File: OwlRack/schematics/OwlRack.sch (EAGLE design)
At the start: 77 parts, among them IC1 THAT1646, IC2 THAT1646, IC3 LM317MABT, IC5 NE5532N, J4 NEUTRIK_NMJ6HCD2, J5 NEUTRIK_NMJ6HCD2

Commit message: changed connector and 5v reg
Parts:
- removed C18: 1u, rcl:CPOL-EUE2.5-7
- removed IC3: LM317MABT, v-reg:LM317MABT
- removed J5: NEUTRIK_NMJ6HCD2, neutrik_jacks:NEUTRIK_NMJ6HCD2
- removed LEFT, RIGHT: NCJ10FI-H, con-neutrik_ag:NCJ10FI-H
- removed R6: 1k, Rebel:R-EU_0204/7
- removed R7: 330R, Rebel:R-EU_0204/7
- added IN3: (no value), SparkFun:M02PTH
- added J1, J2, J3: NEUTRIK_NRJ6HFSTD, neutrik_jacks:NEUTRIK_NRJ6HFSTD
- added U$2: REG_S9V11F5, Rebel:REG_S9V11F5
- J4: value NEUTRIK_NMJ6HCD2 -> NEUTRIK_NRJ6HFSTD; device neutrik_jacks:NEUTRIK_NMJ6HCD2 -> neutrik_jacks:NEUTRIK_NRJ6HFSTD
- UART: device SparkFun:M03PTH -> Rebel:CON-JST-1X03PH-TH
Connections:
- removed net N$11: C18.+, IC3.ADJ, R6.2, R7.1
- new net N$6: J1.R, J2.TN
- net +12V: now also U$2.VIN; no longer IC3.IN
- net +5V: now also U$2.VOUT; no longer IC3.OUT, R7.2
- net FX_IN_L: now also J1.T; no longer J4.T, J5.TN
- net FX_IN_R: now also J2.T; no longer J5.T
- net GND: now also IN3.2, U$2.GND; no longer C18.-, J4.S, J4.TN, J5.S, R300.1, R301.1, R6.1
- net GNDA: now also IN3.1, J1.RN, J1.S, J1.SN, J1.TN, J2.RN, J2.S, J2.SN, J3.S, J4.S, R300.1, R301.1; no longer LEFT.1, LEFT.G, LEFT.S, LEFT.SS, RIGHT.1, RIGHT.G, RIGHT.S, RIGHT.SS
- net N$18: now also J3.R; no longer RIGHT.2, RIGHT.T
- net N$19: now also J3.T; no longer RIGHT.3, RIGHT.R
- net N$2: now also J4.R; no longer LEFT.2, LEFT.T
- net N$3: now also J4.T; no longer LEFT.3, LEFT.R
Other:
- note added: "Copyright 2017 Rebel Technology"
- note added: "OWL Rack Rev03"
- note removed: "Copyright 2016 Rebel Technology"
- note removed: "OWL Rack Revision 2"
- moved on the sheet: C1, C10, C11, C12, C13, C14, C15, C16, C2, C3, C300, C301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

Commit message: boards sent for production
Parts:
- added IN4, IN5: (no value), SparkFun:M02PTH
- renumbered U$2 to IC3
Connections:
- net GND: now also IN4.2, IN5.2
- net GNDA: now also IN4.1, IN5.1
- net N$18: now also J4.R; no longer J3.R
- net N$19: now also J4.T; no longer J3.T
- net N$2: now also J3.R; no longer J4.R
- net N$3: now also J3.T; no longer J4.T
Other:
- moved on the sheet: J3, J4
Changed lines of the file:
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@@
 <part name="J1" library="neutrik_jacks" deviceset="NEUTRIK_NRJ6HF" device="STD"/>
 <part name="J2" library="neutrik_jacks" deviceset="NEUTRIK_NRJ6HF" device="STD"/>
+<part name="J4" library="neutrik_jacks" deviceset="NEUTRIK_NRJ6HF" device="STD"/>
 <part name="J3" library="neutrik_jacks" deviceset="NEUTRIK_NRJ6HF" device="STD"/>
-<part name="J4" library="neutrik_jacks" deviceset="NEUTRIK_NRJ6HF" device="STD"/>
 <part name="UART" library="Rebel" deviceset="CON-JST-1X03" device="PH-TH"/>
-<part name="U$2" library="Rebel" deviceset="REG_S9V11F5" device=""/>
+<part name="IC3" library="Rebel" deviceset="REG_S9V11F5" device=""/>
 <part name="GND5" library="supply1" deviceset="GNDA" device=""/>
 <part name="GND17" library="supply1" deviceset="GNDA" device=""/>
@@
 <part name="GND22" library="supply1" deviceset="GND" device=""/>
 <part name="GND35" library="supply1" deviceset="GNDA" device=""/>
+<part name="IN4" library="SparkFun" deviceset="M02" device="PTH"/>
+<part name="IN5" library="SparkFun" deviceset="M02" device="PTH"/>
 </parts>
 <sheets>
@@
 <instance part="J1" gate="J" x="-45.72" y="101.6"/>
 <instance part="J2" gate="J" x="-45.72" y="55.88"/>
-<instance part="J3" gate="J" x="360.68" y="162.56" rot="R180"/>
-<instance part="J4" gate="J" x="360.68" y="83.82" rot="R180"/>
+<instance part="J4" gate="J" x="360.68" y="162.56" rot="R180"/>
+<instance part="J3" gate="J" x="360.68" y="83.82" rot="R180"/>
 <instance part="UART" gate="G$1" x="195.58" y="81.28"/>
-<instance part="U$2" gate="G$1" x="71.12" y="177.8"/>
+<instance part="IC3" gate="G$1" x="71.12" y="177.8"/>
 <instance part="GND5" gate="1" x="-10.16" y="81.28"/>
 <instance part="GND17" gate="1" x="-33.02" y="35.56"/>
@@
 <instance part="GND22" gate="1" x="-7.62" y="-12.7" rot="MR0"/>
 <instance part="GND35" gate="1" x="-12.7" y="-12.7"/>
+<instance part="IN4" gate="G$1" x="5.08" y="-5.08" rot="R180"/>
+<instance part="IN5" gate="G$1" x="5.08" y="-22.86" rot="R180"/>
 </instances>
 <busses>
@@
 <pinref part="IN2" gate="G$1" pin="2"/>
 <pinref part="GND23" gate="1" pin="GND"/>
-<wire x1="-5.08" y1="-25.4" x2="-7.62" y2="-25.4" width="0.1524" layer="91"/>
+<wire x1="-2.54" y1="-25.4" x2="-7.62" y2="-25.4" width="0.1524" layer="91"/>
 <wire x1="-7.62" y1="-25.4" x2="-7.62" y2="-27.94" width="0.1524" layer="91"/>
+<pinref part="IN5" gate="G$1" pin="2"/>
+<junction x="-2.54" y="-25.4"/>
+<wire x1="-2.54" y1="-25.4" x2="-5.08" y2="-25.4" width="0.1524" layer="91"/>
 </segment>
 <segment>
@@
 </segment>
 <segment>
-<pinref part="U$2" gate="G$1" pin="GND"/>
+<pinref part="IC3" gate="G$1" pin="GND"/>
 <pinref part="GND25" gate="1" pin="GND"/>
 <wire x1="81.28" y1="147.32" x2="81.28" y2="165.1" width="0.1524" layer="91"/>
@@
 <pinref part="IN3" gate="G$1" pin="2"/>
 <pinref part="GND22" gate="1" pin="GND"/>
-<wire x1="-5.08" y1="-7.62" x2="-7.62" y2="-7.62" width="0.1524" layer="91"/>
+<wire x1="-2.54" y1="-7.62" x2="-7.62" y2="-7.62" width="0.1524" layer="91"/>
 <wire x1="-7.62" y1="-7.62" x2="-7.62" y2="-10.16" width="0.1524" layer="91"/>
+<pinref part="IN4" gate="G$1" pin="2"/>
+<junction x="-2.54" y="-7.62"/>
+<wire x1="-2.54" y1="-7.62" x2="-5.08" y2="-7.62" width="0.1524" layer="91"/>
 </segment>
 </net>
@@
 <junction x="96.52" y="177.8"/>
 <pinref part="C17" gate="G$1" pin="+"/>
-<pinref part="U$2" gate="G$1" pin="VOUT"/>
+<pinref part="IC3" gate="G$1" pin="VOUT"/>
 </segment>
 </net>
@@
 <pinref part="P+9" gate="1" pin="+12V"/>
 <pinref part="C19" gate="G$1" pin="1"/>
-<pinref part="U$2" gate="G$1" pin="VIN"/>
+<pinref part="IC3" gate="G$1" pin="VIN"/>
 </segment>
 <segment>
@@
 <wire x1="353.06" y1="154.94" x2="347.98" y2="154.94" width="0.1524" layer="91"/>
 <pinref part="GND11" gate="1" pin="GNDA"/>
-<pinref part="J3" gate="J" pin="S"/>
+<pinref part="J4" gate="J" pin="S"/>
 </segment>
 <segment>
@@
 <wire x1="353.06" y1="76.2" x2="347.98" y2="76.2" width="0.1524" layer="91"/>
 <wire x1="347.98" y1="76.2" x2="347.98" y2="71.12" width="0.1524" layer="91"/>
-<pinref part="J4" gate="J" pin="S"/>
+<pinref part="J3" gate="J" pin="S"/>
 </segment>
 <segment>
 <pinref part="IN2" gate="G$1" pin="1"/>
 <pinref part="GND24" gate="1" pin="GNDA"/>
-<wire x1="-5.08" y1="-22.86" x2="-12.7" y2="-22.86" width="0.1524" layer="91"/>
+<wire x1="-2.54" y1="-22.86" x2="-12.7" y2="-22.86" width="0.1524" layer="91"/>
 <wire x1="-12.7" y1="-22.86" x2="-12.7" y2="-27.94" width="0.1524" layer="91"/>
+<pinref part="IN5" gate="G$1" pin="1"/>
+<junction x="-2.54" y="-22.86"/>
+<wire x1="-2.54" y1="-22.86" x2="-5.08" y2="-22.86" width="0.1524" layer="91"/>
 </segment>
 <segment>
@@
 <pinref part="IN3" gate="G$1" pin="1"/>
 <pinref part="GND35" gate="1" pin="GNDA"/>
-<wire x1="-5.08" y1="-5.08" x2="-12.7" y2="-5.08" width="0.1524" layer="91"/>
+<wire x1="-2.54" y1="-5.08" x2="-12.7" y2="-5.08" width="0.1524" layer="91"/>
 <wire x1="-12.7" y1="-5.08" x2="-12.7" y2="-10.16" width="0.1524" layer="91"/>
+<pinref part="IN4" gate="G$1" pin="1"/>
+<junction x="-2.54" y="-5.08"/>
+<wire x1="-2.54" y1="-5.08" x2="-5.08" y2="-5.08" width="0.1524" layer="91"/>
 </segment>
 </net>
@@
 <wire x1="317.5" y1="167.64" x2="317.5" y2="160.02" width="0.1524" layer="91"/>
 <junction x="317.5" y="160.02"/>
-<pinref part="J3" gate="J" pin="R"/>
+<pinref part="J4" gate="J" pin="R"/>
 </segment>
 </net>
@@
 <wire x1="266.7" y1="167.64" x2="266.7" y2="165.1" width="0.1524" layer="91"/>
 <junction x="266.7" y="165.1"/>
-<pinref part="J3" gate="J" pin="T"/>
+<pinref part="J4" gate="J" pin="T"/>
 </segment>
 </net>
@@
 <wire x1="320.04" y1="88.9" x2="320.04" y2="81.28" width="0.1524" layer="91"/>
 <junction x="320.04" y="81.28"/>
-<pinref part="J4" gate="J" pin="R"/>
+<pinref part="J3" gate="J" pin="R"/>
 </segment>
 </net>
@@
 <wire x1="269.24" y1="88.9" x2="269.24" y2="86.36" width="0.1524" layer="91"/>
 <junction x="269.24" y="86.36"/>
-<pinref part="J4" gate="J" pin="T"/>
-</segment>
-</net>
+<pinref part="J3" gate="J" pin="T"/>
+</segment>
+</net>

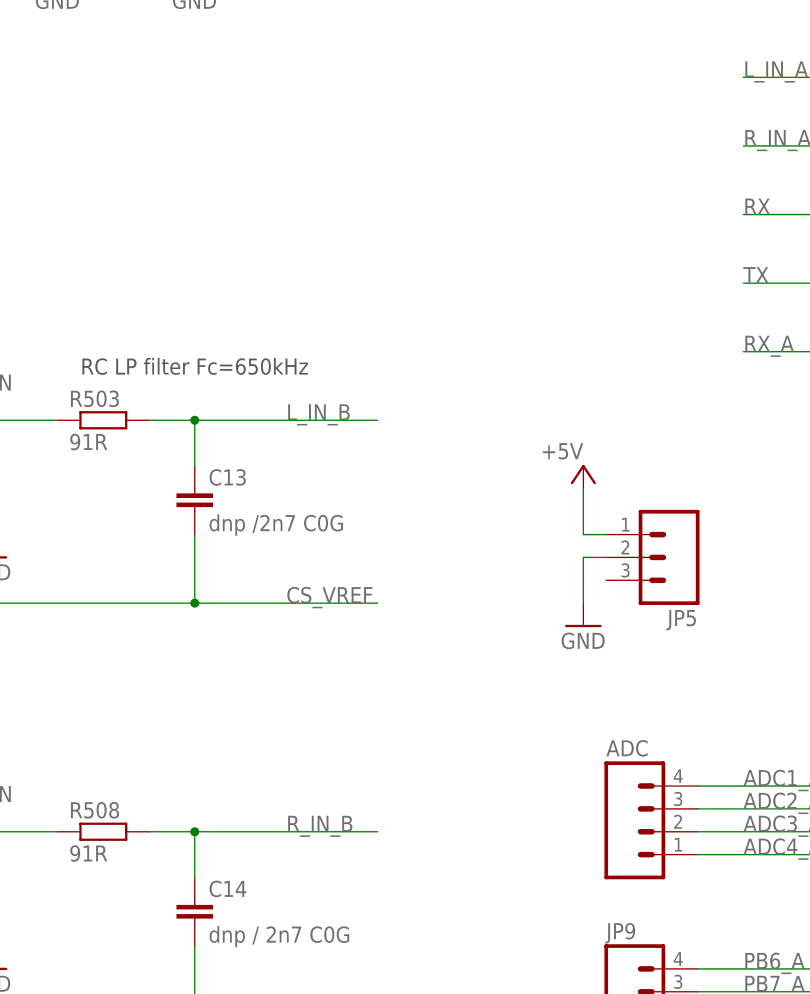
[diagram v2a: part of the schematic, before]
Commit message: Fixed mechanical OWL top board and both OWL rack boards.
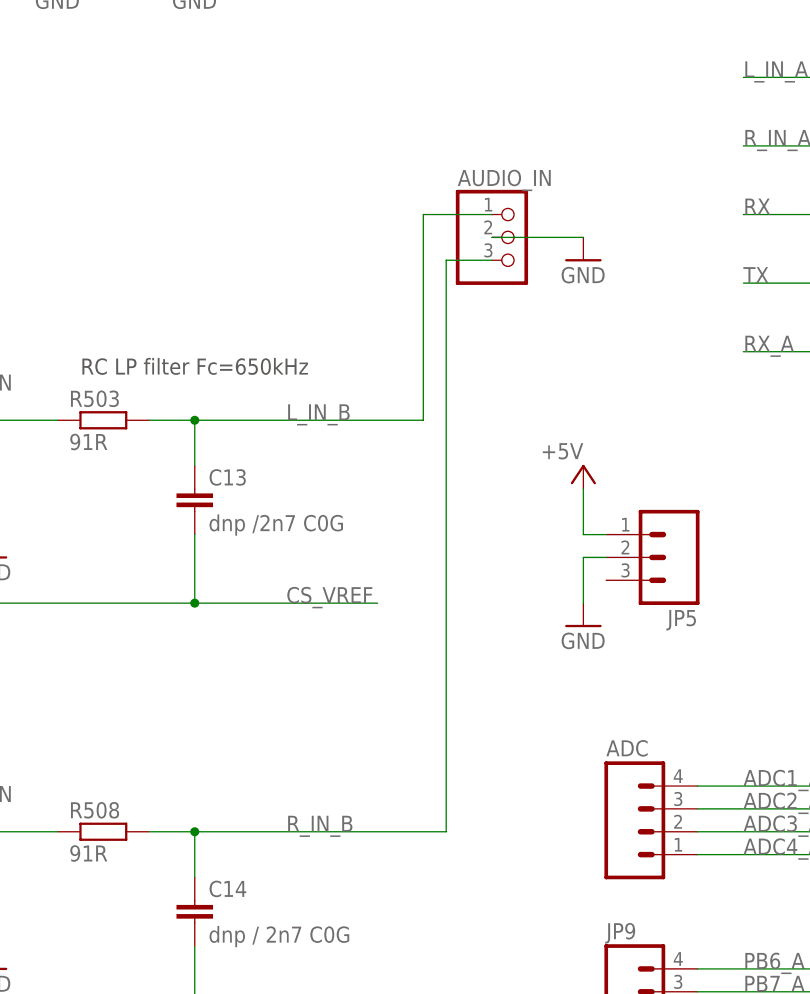
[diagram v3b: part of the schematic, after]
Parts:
- added AUDIO_IN: (no value), Rebel:CON-JST-1X03PH-TH
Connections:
- net GND: now also AUDIO_IN.2
- net L_IN_B: now also AUDIO_IN.1
- net R_IN_B: now also AUDIO_IN.3
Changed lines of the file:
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@@
 <?xml version="1.0" encoding="utf-8"?>
 <!DOCTYPE eagle SYSTEM "eagle.dtd">
-<eagle version="7.5.0">
+<eagle version="7.6.0">
 <drawing>
 <settings>
@@
 <part name="IN4" library="SparkFun" deviceset="M02" device="PTH"/>
 <part name="IN5" library="SparkFun" deviceset="M02" device="PTH"/>
+<part name="AUDIO_IN" library="Rebel" deviceset="CON-JST-1X03" device="PH-TH"/>
+<part name="GND36" library="supply1" deviceset="GND" device=""/>
 </parts>
 <sheets>
@@
 <instance part="IN4" gate="G$1" x="5.08" y="-5.08" rot="R180"/>
 <instance part="IN5" gate="G$1" x="5.08" y="-22.86" rot="R180"/>
+<instance part="AUDIO_IN" gate="G$1" x="132.08" y="116.84"/>
+<instance part="GND36" gate="1" x="139.7" y="114.3"/>
 </instances>
 <busses>
@@
 <wire x1="-2.54" y1="-7.62" x2="-5.08" y2="-7.62" width="0.1524" layer="91"/>
 </segment>
+<segment>
+<pinref part="AUDIO_IN" gate="G$1" pin="2"/>
+<pinref part="GND36" gate="1" pin="GND"/>
+<wire x1="129.54" y1="116.84" x2="139.7" y2="116.84" width="0.1524" layer="91"/>
+</segment>
 </net>
 <net name="+5V" class="0">
@@
 <wire x1="96.52" y1="45.72" x2="96.52" y2="50.8" width="0.1524" layer="91"/>
 <junction x="96.52" y="50.8"/>
-<wire x1="96.52" y1="50.8" x2="116.84" y2="50.8" width="0.1524" layer="91"/>
+<wire x1="96.52" y1="50.8" x2="124.46" y2="50.8" width="0.1524" layer="91"/>
 <pinref part="C14" gate="G$1" pin="1"/>
+<wire x1="124.46" y1="50.8" x2="124.46" y2="114.3" width="0.1524" layer="91"/>
+<pinref part="AUDIO_IN" gate="G$1" pin="3"/>
+<wire x1="124.46" y1="114.3" x2="129.54" y2="114.3" width="0.1524" layer="91"/>
 </segment>
 </net>
@@
 <junction x="96.52" y="96.52"/>
 <pinref part="R503" gate="G$1" pin="2"/>
-<wire x1="96.52" y1="96.52" x2="116.84" y2="96.52" width="0.1524" layer="91"/>
+<wire x1="96.52" y1="96.52" x2="121.92" y2="96.52" width="0.1524" layer="91"/>
 <pinref part="C13" gate="G$1" pin="1"/>
-</segment>
-</net>
+<wire x1="121.92" y1="96.52" x2="121.92" y2="119.38" width="0.1524" layer="91"/>
+<pinref part="AUDIO_IN" gate="G$1" pin="1"/>
+<wire x1="121.92" y1="119.38" x2="129.54" y2="119.38" width="0.1524" layer="91"/>
+</segment>
+</net>

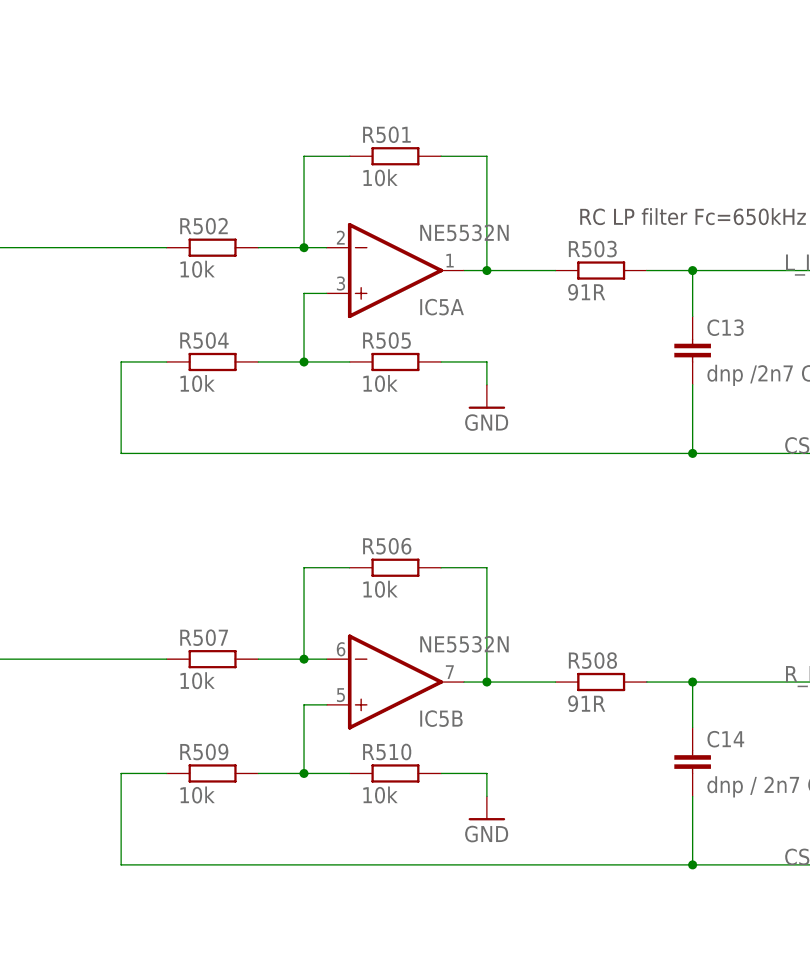
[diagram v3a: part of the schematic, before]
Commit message: changed component values
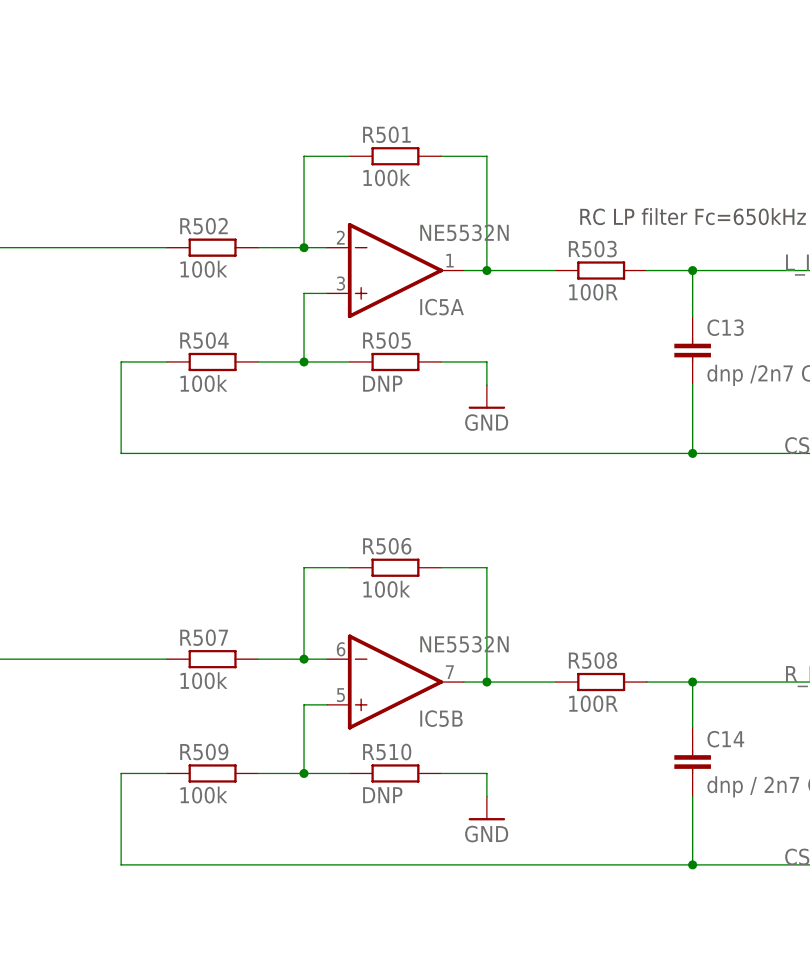
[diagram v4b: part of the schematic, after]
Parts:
- R501, R502, R504, R506, R507, R509: value 10k -> 100k
- R503, R508: value 91R -> 100R
- R505, R510: value 10k -> DNP
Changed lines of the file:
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@@
 <?xml version="1.0" encoding="utf-8"?>
 <!DOCTYPE eagle SYSTEM "eagle.dtd">
-<eagle version="7.6.0">
+<eagle version="7.5.0">
 <drawing>
 <settings>
@@
 <part name="JP11" library="SparkFun" deviceset="M02" device="PTH"/>
 <part name="JP12" library="SparkFun" deviceset="M04" device="PTH"/>
-<part name="R508" library="Rebel" deviceset="R-EU_" device="0204/7" value="91R"/>
-<part name="R503" library="Rebel" deviceset="R-EU_" device="0204/7" value="91R"/>
+<part name="R508" library="Rebel" deviceset="R-EU_" device="0204/7" value="100R"/>
+<part name="R503" library="Rebel" deviceset="R-EU_" device="0204/7" value="100R"/>
 <part name="GND26" library="supply1" deviceset="GND" device=""/>
 <part name="GND27" library="supply1" deviceset="GND" device=""/>
 <part name="P+6" library="supply1" deviceset="+12V" device=""/>
 <part name="P-1" library="supply1" deviceset="-12V" device=""/>
-<part name="R501" library="Rebel" deviceset="R-EU_" device="0204/7" value="10k"/>
-<part name="R504" library="Rebel" deviceset="R-EU_" device="0204/7" value="10k"/>
-<part name="R505" library="Rebel" deviceset="R-EU_" device="0204/7" value="10k"/>
-<part name="R502" library="Rebel" deviceset="R-EU_" device="0204/7" value="10k"/>
+<part name="R501" library="Rebel" deviceset="R-EU_" device="0204/7" value="100k"/>
+<part name="R504" library="Rebel" deviceset="R-EU_" device="0204/7" value="100k"/>
+<part name="R505" library="Rebel" deviceset="R-EU_" device="0204/7" value="DNP"/>
+<part name="R502" library="Rebel" deviceset="R-EU_" device="0204/7" value="100k"/>
 <part name="GND2" library="supply1" deviceset="GND" device=""/>
-<part name="R506" library="Rebel" deviceset="R-EU_" device="0204/7" value="10k"/>
-<part name="R509" library="Rebel" deviceset="R-EU_" device="0204/7" value="10k"/>
-<part name="R510" library="Rebel" deviceset="R-EU_" device="0204/7" value="10k"/>
-<part name="R507" library="Rebel" deviceset="R-EU_" device="0204/7" value="10k"/>
+<part name="R506" library="Rebel" deviceset="R-EU_" device="0204/7" value="100k"/>
+<part name="R509" library="Rebel" deviceset="R-EU_" device="0204/7" value="100k"/>
+<part name="R510" library="Rebel" deviceset="R-EU_" device="0204/7" value="DNP"/>
+<part name="R507" library="Rebel" deviceset="R-EU_" device="0204/7" value="100k"/>
 <part name="GND6" library="supply1" deviceset="GND" device=""/>
 <part name="IC5" library="linear" deviceset="NE5532" device="N" value="NE5532N"/>
